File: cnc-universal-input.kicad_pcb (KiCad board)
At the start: 2 copper layers, 96.5 x 96.5 mm, 123 parts, among them J1 3PT, J10 2PT, J11 8PT, J12 USB_B_Mini, J13 2PT, J14 2PT, J2 3PT, J3 3PT, J4 3PT, J5 3PT, J6 3PT, J7 3PT, J8 3PT, J9 AVR-ISP-6, Q1 2N7002, Q11 2N7002, Q12 2N7002, Q13 2N7002, SW1 RESET, SW2 BTN, U1 ATmega328PB-AU, U10 SFH617A-4, U11 SFH617A-4, U12 SFH617A-4, U13 SFH617A-4, U14 SFH617A-4, U15 SFH617A-4, U16 SFH617A-4, U18 CH340G, U19 TS2596S, U2 74HC595, U3 74HC595, U4 74HC595, U5 4051, U6 TS2596S, U8 LM7321, U9 SFH617A-4, Y1 16MHz, Y2 12MHz

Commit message: Fixed missing and broken step files
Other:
- board text added: "IvyBit"
- board text added: "v1.5"
- board text removed: "IvyBit 2021"
- board text removed: "v1.4"
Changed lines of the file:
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@@
-(kicad_pcb (version 20171130) (host pcbnew "(5.1.8)-1")
+(kicad_pcb (version 20171130) (host pcbnew "(5.1.5)-3")
   (general
     (thickness 1.6)
@@
     (solder_mask_min_width 0.25)
     (aux_axis_origin 0 0)
-    (visible_elements 7FFFFFFF)
+    (visible_elements 7FFDFFFF)
     (pcbplotparams
       (layerselection 0x010fc_ffffffff)
@@
     (pad 1 smd rect (at -1.85 1.15 270) (size 1.9 1.1) (layers F.Cu F.Paste F.Mask)
       (net 2 "Net-(C2-Pad2)"))
-    (model ${KISYS3DMOD}/Crystal.3dshapes/Crystal_SMD_EuroQuartz_MJ-4Pin_5.0x3.2mm.wrl
+    (model ${KISYS3DMOD}/Crystal.3dshapes/Crystal_SMD_3225-4Pin_3.2x2.5mm.step
       (at (xyz 0 0 0))
-      (scale (xyz 1 1 1))
+      (scale (xyz 1.7 1.3 1))
       (rotate (xyz 0 0 0))
     )
@@
     (pad 1 smd rect (at -2.75 0 270) (size 1.5 2.4) (layers F.Cu F.Paste F.Mask)
       (net 78 "Net-(D21-Pad1)"))
-    (model ${KISYS3DMOD}/Inductor_SMD.3dshapes/L_6.3x6.3_H3.wrl
+    (model ${USERMOD}/Inductor_CD32.STEP
       (at (xyz 0 0 0))
-      (scale (xyz 1 1 1))
-      (rotate (xyz 0 0 0))
+      (scale (xyz 1.9 1.9 1.9))
+      (rotate (xyz 0 0 -90))
     )
   )
@@
     (pad 1 smd rect (at -2.75 0 90) (size 1.5 2.4) (layers F.Cu F.Paste F.Mask)
       (net 77 "Net-(D20-Pad1)"))
-    (model ${KISYS3DMOD}/Inductor_SMD.3dshapes/L_6.3x6.3_H3.wrl
+    (model ${USERMOD}/Inductor_CD32.STEP
       (at (xyz 0 0 0))
-      (scale (xyz 1 1 1))
-      (rotate (xyz 0 0 0))
+      (scale (xyz 1.8 1.8 1.8))
+      (rotate (xyz 0 0 -90))
     )
   )
@@
     (pad 1 thru_hole rect (at 0 0) (size 2.5 2.5) (drill 1.3) (layers *.Cu *.Mask)
       (net 4 +12V))
-    (model ${KISYS3DMOD}/TerminalBlock_RND.3dshapes/TerminalBlock_RND_205-00001_1x02_P5.00mm_Horizontal.wrl
-      (at (xyz 0 0 0))
+    (model "${USERMOD}/2er Terminal Block.step"
+      (offset (xyz 5 0 0))
       (scale (xyz 1 1 1))
-      (rotate (xyz 0 0 0))
+      (rotate (xyz 0 0 -180))
     )
   )
@@
     (pad 1 smd roundrect (at -2.625 -1.905 270) (size 1.65 0.6) (layers F.Cu F.Paste F.Mask) (roundrect_rratio 0.25)
       (net 3 +24V))
-    (model ${KISYS3DMOD}/Package_SO.3dshapes/SOP-8_3.9x4.9mm_P1.27mm.wrl
+    (model ${KISYS3DMOD}/Package_SO.3dshapes/SO-8_5.3x6.2mm_P1.27mm.wrl
       (at (xyz 0 0 0))
-      (scale (xyz 1 1 1))
+      (scale (xyz 0.8 1 0.5))
       (rotate (xyz 0 0 0))
     )
@@
     (pad 1 smd roundrect (at -2.625 -1.905 270) (size 1.65 0.6) (layers F.Cu F.Paste F.Mask) (roundrect_rratio 0.25)
       (net 3 +24V))
-    (model ${KISYS3DMOD}/Package_SO.3dshapes/SOP-8_3.9x4.9mm_P1.27mm.wrl
+    (model ${KISYS3DMOD}/Package_SO.3dshapes/SO-8_5.3x6.2mm_P1.27mm.wrl
       (at (xyz 0 0 0))
-      (scale (xyz 1 1 1))
+      (scale (xyz 0.8 1 0.5))
       (rotate (xyz 0 0 0))
     )
@@
     (pad 1 thru_hole rect (at 0 0) (size 2.5 2.5) (drill 1.3) (layers *.Cu *.Mask)
       (net 52 +5VD))
-    (model ${KISYS3DMOD}/TerminalBlock_RND.3dshapes/TerminalBlock_RND_205-00001_1x02_P5.00mm_Horizontal.wrl
-      (at (xyz 0 0 0))
+    (model "${USERMOD}/2er Terminal Block.step"
+      (offset (xyz 5 0 0))
       (scale (xyz 1 1 1))
-      (rotate (xyz 0 0 0))
+      (rotate (xyz 0 0 -180))
     )
   )
@@
     (pad 1 smd rect (at -3.975 -2.25 90) (size 1.55 1.3) (layers F.Cu F.Paste F.Mask)
       (net 1 GND))
-    (model ${KISYS3DMOD}/Button_Switch_SMD.3dshapes/SW_SPST_B3S-1000.wrl
+    (model ${USERMOD}/button_smd_6x6x4.3.stp
       (at (xyz 0 0 0))
       (scale (xyz 1 1 1))
-      (rotate (xyz 0 0 0))
+      (rotate (xyz 0 0 -90))
     )
   )
@@
     (pad 1 smd rect (at -3.975 -2.25 90) (size 1.55 1.3) (layers F.Cu F.Paste F.Mask)
       (net 1 GND))
-    (model ${KISYS3DMOD}/Button_Switch_SMD.3dshapes/SW_SPST_B3S-1000.wrl
+    (model ${USERMOD}/button_smd_6x6x4.3.stp
       (at (xyz 0 0 0))
       (scale (xyz 1 1 1))
-      (rotate (xyz 0 0 0))
+      (rotate (xyz 0 0 -90))
     )
   )
@@
     (pad 1 thru_hole rect (at 0 0) (size 2.5 2.5) (drill 1.3) (layers *.Cu *.Mask)
       (net 93 /BA))
-    (model ${KISYS3DMOD}/TerminalBlock_RND.3dshapes/TerminalBlock_RND_205-00007_1x08_P5.00mm_Horizontal.wrl
-      (at (xyz 0 0 0))
+    (model "${USERMOD}/8er Terminal Block.step"
+      (offset (xyz 35.2 0 0))
       (scale (xyz 1 1 1))
-      (rotate (xyz 0 0 0))
+      (rotate (xyz 0 0 -180))
     )
   )
@@
     (pad 1 thru_hole rect (at 0 0) (size 2.5 2.5) (drill 1.3) (layers *.Cu *.Mask)
       (net 3 +24V))
-    (model ${KISYS3DMOD}/TerminalBlock_RND.3dshapes/TerminalBlock_RND_205-00001_1x02_P5.00mm_Horizontal.wrl
-      (at (xyz 0 0 0))
+    (model "${USERMOD}/2er Terminal Block.step"
+      (offset (xyz 5 0 0))
       (scale (xyz 1 1 1))
-      (rotate (xyz 0 0 0))
+      (rotate (xyz 0 0 -180))
     )
   )
@@
     (pad 1 thru_hole rect (at 0 0 90) (size 2.5 2.5) (drill 1.3) (layers *.Cu *.Mask)
       (net 1 GND))
-    (model ${KISYS3DMOD}/TerminalBlock_RND.3dshapes/TerminalBlock_RND_205-00013_1x03_P5.00mm_Horizontal.wrl
-      (at (xyz 0 0 0))
+    (model "${USERMOD}/3er Terminal Block.step"
+      (offset (xyz 10 0 0))
       (scale (xyz 1 1 1))
-      (rotate (xyz 0 0 0))
+      (rotate (xyz 0 0 -180))
     )
   )
@@
     (pad 1 thru_hole rect (at 0 0 90) (size 2.5 2.5) (drill 1.3) (layers *.Cu *.Mask)
       (net 1 GND))
-    (model ${KISYS3DMOD}/TerminalBlock_RND.3dshapes/TerminalBlock_RND_205-00013_1x03_P5.00mm_Horizontal.wrl
-      (at (xyz 0 0 0))
+    (model "${USERMOD}/3er Terminal Block.step"
+      (offset (xyz 10 0 0))
       (scale (xyz 1 1 1))
-      (rotate (xyz 0 0 0))
+      (rotate (xyz 0 0 -180))
     )
   )
@@
     (pad 1 thru_hole rect (at 0 0 180) (size 2.5 2.5) (drill 1.3) (layers *.Cu *.Mask)
       (net 1 GND))
-    (model ${KISYS3DMOD}/TerminalBlock_RND.3dshapes/TerminalBlock_RND_205-00013_1x03_P5.00mm_Horizontal.wrl
-      (at (xyz 0 0 0))
+    (model "${USERMOD}/3er Terminal Block.step"
+      (offset (xyz 10 0 0))
       (scale (xyz 1 1 1))
-      (rotate (xyz 0 0 0))
+      (rotate (xyz 0 0 180))
     )
   )
@@
     (pad 1 thru_hole rect (at 0 0 180) (size 2.5 2.5) (drill 1.3) (layers *.Cu *.Mask)
       (net 1 GND))
-    (model ${KISYS3DMOD}/TerminalBlock_RND.3dshapes/TerminalBlock_RND_205-00013_1x03_P5.00mm_Horizontal.wrl
-      (at (xyz 0 0 0))
+    (model "${USERMOD}/3er Terminal Block.step"
+      (offset (xyz 10 0 0))
       (scale (xyz 1 1 1))
-      (rotate (xyz 0 0 0))
+      (rotate (xyz 0 0 -180))
     )
   )
@@
     (pad 1 thru_hole rect (at 0 0 180) (size 2.5 2.5) (drill 1.3) (layers *.Cu *.Mask)
       (net 1 GND))
-    (model ${KISYS3DMOD}/TerminalBlock_RND.3dshapes/TerminalBlock_RND_205-00013_1x03_P5.00mm_Horizontal.wrl
-      (at (xyz 0 0 0))
+    (model "${USERMOD}/3er Terminal Block.step"
+      (offset (xyz 10 0 0))
       (scale (xyz 1 1 1))
-      (rotate (xyz 0 0 0))
+      (rotate (xyz 0 0 -180))
     )
   )
@@
     (pad 1 thru_hole rect (at 0 0 180) (size 2.5 2.5) (drill 1.3) (layers *.Cu *.Mask)
       (net 1 GND))
-    (model ${KISYS3DMOD}/TerminalBlock_RND.3dshapes/TerminalBlock_RND_205-00013_1x03_P5.00mm_Horizontal.wrl
-      (at (xyz 0 0 0))
+    (model "${USERMOD}/3er Terminal Block.step"
+      (offset (xyz 10 0 0))
       (scale (xyz 1 1 1))
-      (rotate (xyz 0 0 0))
+      (rotate (xyz 0 0 -180))
     )
   )
@@
     (pad 1 thru_hole rect (at 0 0 270) (size 2.5 2.5) (drill 1.3) (layers *.Cu *.Mask)
       (net 1 GND))
-    (model ${KISYS3DMOD}/TerminalBlock_RND.3dshapes/TerminalBlock_RND_205-00013_1x03_P5.00mm_Horizontal.wrl
-      (at (xyz 0 0 0))
+    (model "${USERMOD}/3er Terminal Block.step"
+      (offset (xyz 10 0 0))
       (scale (xyz 1 1 1))
-      (rotate (xyz 0 0 0))
+      (rotate (xyz 0 0 -180))
     )
   )
@@
     (pad 1 thru_hole rect (at 0 0 270) (size 2.5 2.5) (drill 1.3) (layers *.Cu *.Mask)
       (net 1 GND))
-    (model ${KISYS3DMOD}/TerminalBlock_RND.3dshapes/TerminalBlock_RND_205-00013_1x03_P5.00mm_Horizontal.wrl
-      (at (xyz 0 0 0))
+    (model "${USERMOD}/3er Terminal Block.step"
+      (offset (xyz 10 0 0))
       (scale (xyz 1 1 1))
-      (rotate (xyz 0 0 0))
+      (rotate (xyz 0 0 -180))
     )
   )
@@
   (gr_circle (center 229.108 -77.216) (end 229.362 -77.216) (layer F.SilkS) (width 0.5))
   (gr_circle (center 250.19 -54.61) (end 250.444 -54.61) (layer F.SilkS) (width 0.5))
-  (gr_text "IvyBit 2021" (at 249.174 -59.944) (layer F.Mask)
+  (gr_text IvyBit (at 249.174 -59.944) (layer F.Mask)
     (effects (font (size 1 1) (thickness 0.127)))
   )
@@
     (effects (font (size 1.5 1.5) (thickness 0.3)))
   )
-  (gr_text v1.4 (at 243.078 -59.944) (layer F.Mask)
+  (gr_text v1.5 (at 245.11 -59.944) (layer F.Mask)
     (effects (font (size 1 1) (thickness 0.127)))
   )

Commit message: Cap be gone
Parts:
- removed C25: 10uF, Capacitor_SMD:CP_Elec_4x5.4
- removed C26: 100nF, Capacitor_SMD:C_0805_2012Metric
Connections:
- J12 pad 1: Net-(J12-Pad1) -> (no net)
- J12 pad 4: Net-(J12-Pad4) -> (no net)
- U1 pad 3: Net-(U1-Pad3) -> (no net)
- U1 pad 6: Net-(U1-Pad6) -> (no net)
- U18 pad 10: Net-(U18-Pad10) -> (no net)
- U18 pad 11: Net-(U18-Pad11) -> (no net)
- U18 pad 12: Net-(U18-Pad12) -> (no net)
- U18 pad 13: Net-(U18-Pad13) -> (no net)
- U18 pad 14: Net-(U18-Pad14) -> (no net)
- U18 pad 15: Net-(U18-Pad15) -> (no net)
- U18 pad 9: Net-(U18-Pad9) -> (no net)
- U2 pad 9: Net-(U2-Pad9) -> (no net)
- U3 pad 9: Net-(U3-Pad9) -> (no net)
- U8 pad 1: Net-(U8-Pad1) -> (no net)
- U8 pad 5: Net-(U8-Pad5) -> (no net)
- U8 pad 8: Net-(U8-Pad8) -> (no net)
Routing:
- net +5VD: track 38.1 -> 29.4 mm
- net /BE: track 45.9 -> 45.4 mm

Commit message: vias
removed most vias under pads
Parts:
- moved C6 168.7 mm to (104.3, 122.0)
- moved C1 168.7 mm to (112.6, 87.8)
- moved C10 168.7 mm to (185.0, 94.0)
- moved C11 168.7 mm to (170.3, 94.0)
- moved C12 168.7 mm to (170.3, 109.3)
- moved C13 168.7 mm to (176.0, 94.0)
- moved C14 168.7 mm to (117.0, 113.3)
- moved C19 168.7 mm to (116.9, 83.6)
- moved C22 168.7 mm to (123.4, 57.5)
- moved C23 168.7 mm to (136.0, 69.8)
- moved C3 168.7 mm to (104.3, 114.4)
- moved C5 168.7 mm to (159.8, 56.2)
- moved C7 168.7 mm to (104.3, 106.7)
- moved C8 168.7 mm to (117.0, 115.4)
- moved D10 168.7 mm to (165.9, 68.0)
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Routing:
- net +12V: track 347.4 -> 351.0 mm, vias 11 -> 13
- net /TO: track 22.0 -> 23.6 mm
- net /OUT-E: track 29.3 -> 30.7 mm
- net /OUT-G: track 28.3 -> 29.7 mm
- net /OUT-F: track 28.8 -> 30.1 mm
- net /OUT-H: track 28.4 -> 29.8 mm
- net /OUT-A: track 24.5 -> 25.4 mm
- net /OUT-D: track 26.2 -> 27.1 mm
- net /OUT-C: track 27.4 -> 28.2 mm
- net /OUT-B: track 27.4 -> 28.1 mm

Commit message: assemble all the things!
JLCPCB please make my life easier!!
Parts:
- removed J11: 8PT, TerminalBlock_RND:TerminalBlock_RND_205-00007_1x08_P5.00mm_Horizontal
- removed R72: 4.7K, Resistor_SMD:R_0805_2012Metric
- removed R73: 1.5K, Resistor_SMD:R_0805_2012Metric
- removed R74: 9.1K, Resistor_SMD:R_0805_2012Metric
- removed R75: 1K, Resistor_SMD:R_0805_2012Metric
- removed RN11, RN12: 470P4, Resistor_SMD:R_Array_Convex_4x0603
- added C25: 10uF, Capacitor_SMD:C_1206_3216Metric, F.Cu at (170.2, 96.0)
- added C26: 10uF, Capacitor_SMD:C_1206_3216Metric, F.Cu at (126.0, 45.0)
- added D27: LEDO, Diode_SMD:D_0805_2012Metric, F.Cu at (170.2, 100.6)
- added J15: 2PT, TerminalBlock_RND:TerminalBlock_RND_205-00001_1x02_P5.00mm_Horizontal, F.Cu at (135.3, 132.1)
- added J16: 2PT, TerminalBlock_RND:TerminalBlock_RND_205-00001_1x02_P5.00mm_Horizontal, F.Cu at (145.3, 132.1)
- added J17: 2PT, TerminalBlock_RND:TerminalBlock_RND_205-00001_1x02_P5.00mm_Horizontal, F.Cu at (155.3, 132.1)
- added J18: 2PT, TerminalBlock_RND:TerminalBlock_RND_205-00001_1x02_P5.00mm_Horizontal, F.Cu at (165.3, 132.1)
- added Q2: 2N7002, Package_TO_SOT_SMD:SOT-23, F.Cu at (141.6, 97.5)
- added Q3: 2N7002, Package_TO_SOT_SMD:SOT-23, F.Cu at (141.6, 101.1)
- added Q4: 2N7002, Package_TO_SOT_SMD:SOT-23, F.Cu at (141.6, 104.6)
- added Q5: 2N7002, Package_TO_SOT_SMD:SOT-23, F.Cu at (141.6, 108.2)
- added Q6: 2N7002, Package_TO_SOT_SMD:SOT-23, F.Cu at (141.6, 115.3)
- added Q7: 2N7002, Package_TO_SOT_SMD:SOT-23, F.Cu at (141.6, 111.8)
- added Q8: 2N7002, Package_TO_SOT_SMD:SOT-23, F.Cu at (141.6, 118.9)
- added Q9: 2N7002, Package_TO_SOT_SMD:SOT-23, F.Cu at (141.6, 122.4)
- added R1: 220, Resistor_SMD:R_0805_2012Metric, F.Cu at (162.6, 102.2)
- added R2: 220, Resistor_SMD:R_0805_2012Metric, F.Cu at (157.5, 102.2)
- added R3: 220, Resistor_SMD:R_0805_2012Metric, F.Cu at (152.4, 102.2)
- added R4: 220, Resistor_SMD:R_0805_2012Metric, F.Cu at (147.3, 102.2)
- added R5: 220, Resistor_SMD:R_0805_2012Metric, F.Cu at (157.5, 113.7)
- added R6: 220, Resistor_SMD:R_0805_2012Metric, F.Cu at (162.6, 113.7)
- added R7: 220, Resistor_SMD:R_0805_2012Metric, F.Cu at (152.4, 113.7)
- added R8: 220, Resistor_SMD:R_0805_2012Metric, F.Cu at (147.3, 113.7)
- added R9: 1K, Resistor_SMD:R_0805_2012Metric, F.Cu at (170.2, 98.3)
- added TP1: GND, TestPoint:TestPoint_Pad_D1.5mm, F.Cu at (113.0, 57.1)
- added TP2: +24V, TestPoint:TestPoint_Pad_D1.5mm, F.Cu at (126.4, 57.1)
- added TP3: +5V, TestPoint:TestPoint_Pad_D1.5mm, F.Cu at (117.5, 57.1)
- added TP4: +12V, TestPoint:TestPoint_Pad_D1.5mm, F.Cu at (121.9, 57.1)
- added U7: ADuM1201AR, Package_SO:SOIC-8_3.9x4.9mm_P1.27mm, F.Cu at (177.0, 93.0)
- BZ1: footprint Buzzer_Beeper:MagneticBuzzer_ProSignal_ABT-410-RC -> Buzzer_Beeper:Buzzer_15x7.5RM7.6
- C10, C5: value 10uF -> 100nF; footprint Capacitor_SMD:CP_Elec_4x5.4 -> Capacitor_SMD:C_0805_2012Metric
- C11, C12: value 30pF -> 22pF
- C14, C8: value 100nF -> 10uF; footprint Capacitor_SMD:C_0805_2012Metric -> Capacitor_SMD:C_1206_3216Metric
- C15, C24: value 10nF -> 10uF; footprint Capacitor_SMD:C_0805_2012Metric -> Capacitor_SMD:C_1206_3216Metric
- C22, C27, C28: footprint Capacitor_SMD:CP_Elec_4x5.4 -> Capacitor_SMD:C_1206_3216Metric
- C3: value 150uF -> 470uF; footprint Capacitor_SMD:CP_Elec_6.3x7.7 -> Capacitor_SMD:CP_Elec_10x10
- D20, D21: value B240F -> SS36-E3/57T
- L1, L2: footprint Inductor_SMD:L_6.3x6.3_H3 -> Inductor_SMD:L_12x12mm_H8mm
- RN1, RN2: value 10KP4 -> 4.7KP4
- RN3, RN4: value 470P4 -> 330P4
- RN5, RN6: value 470P4 -> 620P4
- SW1, SW2: footprint Button_Switch_SMD:SW_SPST_B3S-1000 -> Button_Switch_SMD:SW_SPST_TL3342
- U10, U11, U12, U13, U14, U15, U16, U9: value SFH617A-4 -> EL357NC; footprint Package_DIP:DIP-4_W7.62mm -> IvyBit-footprints:SOP-4_4.1x4.4x2.54P
- U19: value TS2596S -> XL1509-5E1; footprint Package_SO:SOP-8_3.9x4.9mm_P1.27mm -> Package_SO:SOIC-8_3.9x4.9mm_P1.27mm
- U6: value TS2596S -> XL1509-12E1; footprint Package_SO:SOP-8_3.9x4.9mm_P1.27mm -> Package_SO:SOIC-8_3.9x4.9mm_P1.27mm
- U8: value LM7321 -> SGMOP07CXS8G/TR
- Y1: footprint Crystal:Crystal_SMD_EuroQuartz_MJ-4Pin_5.0x3.2mm -> Crystal:Crystal_SMD_3225-4Pin_3.2x2.5mm
- Y2: footprint Crystal:Crystal_HC49-4H_Vertical -> Crystal:Crystal_SMD_3225-4Pin_3.2x2.5mm
- moved C14 74.6 mm to (146.3, 44.7), turned to 270 degrees
- moved C24 72.6 mm to (166.6, 45.0), turned to 270 degrees
- moved C5 45.7 mm to (177.0, 98.6), turned to 180 degrees
- moved C8 34.6 mm to (146.8, 97.8)
- moved R17 24.8 mm to (112.6, 78.1)
- moved U9 21.0 mm to (162.6, 108.0)
- moved L1 20.8 mm to (129.5, 104.1), turned to 0 degrees
- moved C15 19.4 mm to (122.2, 96.8), turned to 270 degrees
- moved D21 18.9 mm to (118.1, 122.6), turned to 180 degrees
- moved U10 17.8 mm to (157.5, 108.0)
- moved U19 17.3 mm to (118.1, 105.4), turned to 180 degrees
- moved C6 16.4 mm to (110.2, 106.7), turned to 270 degrees
- moved U15 16.2 mm to (152.4, 119.4)
- moved L2 16.1 mm to (129.5, 118.1), turned to 0 degrees
- moved U13 16.1 mm to (162.6, 119.4)
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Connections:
- C10 pad 1: +5V -> GND
- C10 pad 2: GND -> +5V
- C11 pad 1: GND -> GND_USB
- C12 pad 1: GND -> Net-(C12-Pad1)
- C12 pad 2: Net-(C12-Pad2) -> GND_USB
- C13 pad 2: GND -> GND_USB
- C15 pad 2: Net-(C15-Pad2) -> GND
- C21 pad 1: +5V -> VBUS
- C21 pad 2: GND -> GND_USB
- C24 pad 2: Net-(C24-Pad2) -> GND
- C5 pad 1: +5V -> GND_USB
- C5 pad 2: GND -> VBUS
- D18 pad 1: /RX -> /RX1
- D19 pad 1: /TX -> /TX1
- J12 pad 1: (no net) -> VBUS
- J12 pad 5: GND -> GND_USB
- R66 pad 1: +5V -> VBUS
- R67 pad 1: +5V -> VBUS
- U1 pad 30: /RX -> /RX2
- U1 pad 31: /TX -> /TX2
- U10 pad 1: /POB -> Net-(R2-Pad2)
- U10 pad 2: GND -> Net-(Q3-Pad3)
- U11 pad 1: /POC -> Net-(R3-Pad2)
- U11 pad 2: GND -> Net-(Q4-Pad3)
- U12 pad 1: /POD -> Net-(R4-Pad2)
- U12 pad 2: GND -> Net-(Q5-Pad3)
- U13 pad 1: /POE -> Net-(R6-Pad2)
- U13 pad 2: GND -> Net-(Q7-Pad3)
- U14 pad 1: /POF -> Net-(R5-Pad2)
- U14 pad 2: GND -> Net-(Q6-Pad3)
- U15 pad 1: /POG -> Net-(R7-Pad2)
- U15 pad 2: GND -> Net-(Q8-Pad3)
- U16 pad 1: /POH -> Net-(R8-Pad2)
- U16 pad 2: GND -> Net-(Q9-Pad3)
- U18 pad 1: GND -> GND_USB
- U18 pad 16: +5V -> VBUS
- U18 pad 2: /RX -> /RX1
- U18 pad 3: /TX -> /TX1
- U18 pad 7: Net-(C11-Pad2) -> Net-(C12-Pad1)
- U18 pad 8: Net-(C12-Pad2) -> Net-(C11-Pad2)
- U19 pad 3: Net-(C15-Pad2) -> +5V
- U6 pad 3: Net-(C24-Pad2) -> +12V
- U9 pad 1: /POA -> Net-(R1-Pad2)
- U9 pad 2: GND -> Net-(Q2-Pad3)
- Y2 pad 1: Net-(C12-Pad2) -> Net-(C11-Pad2)
- Y2 pad 2: Net-(C11-Pad2) -> GND_USB
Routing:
- net +5V: track 282.7 -> 377.0 mm
- net /TX: track 80.7 -> 0.00 mm, vias 2 -> 0
- net /RX: track 77.2 -> 0.00 mm, vias 2 -> 0
- net /RX2: track 0.00 -> 65.0 mm, vias 0 -> 2
- net /TX2: track 0.00 -> 64.1 mm, vias 0 -> 2
- net +12V: track 351.0 -> 397.9 mm, vias 13 -> 14
- net GND: track 2.33 -> 47.9 mm, vias 297 -> 252
- net VBUS: track 0.00 -> 40.5 mm, vias 0 -> 1
- net /TX1: track 0.00 -> 29.7 mm, vias 0 -> 2
- net /RX1: track 0.00 -> 29.5 mm, vias 0 -> 2
- net Net-(Q7-Pad3): track 0.00 -> 27.5 mm
- net /BD: track 34.1 -> 60.4 mm, vias 1 -> 2
- net Net-(Q2-Pad3): track 0.00 -> 25.2 mm
- net Net-(Q6-Pad3): track 0.00 -> 24.9 mm
- net Net-(C24-Pad2): track 22.6 -> 0.00 mm
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- added copper zone on B.Cu, net GND_USB
- added copper zone on F.Cu, net GND_USB
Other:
- outline, holes or cut-outs redrawn
- board text added: "15-36V"
- board text added: "3.5mm"
- board text added: "RESET"
- board text added: "v1.6"
- board text removed: "16-30V"
- board text removed: "3.4mm"
- board text removed: "UCNC"
- board text removed: "v1.5"

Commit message: Update cnc-universal-input.kicad_pcb
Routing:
- net /OUT-C: track 26.5 -> 25.9 mm

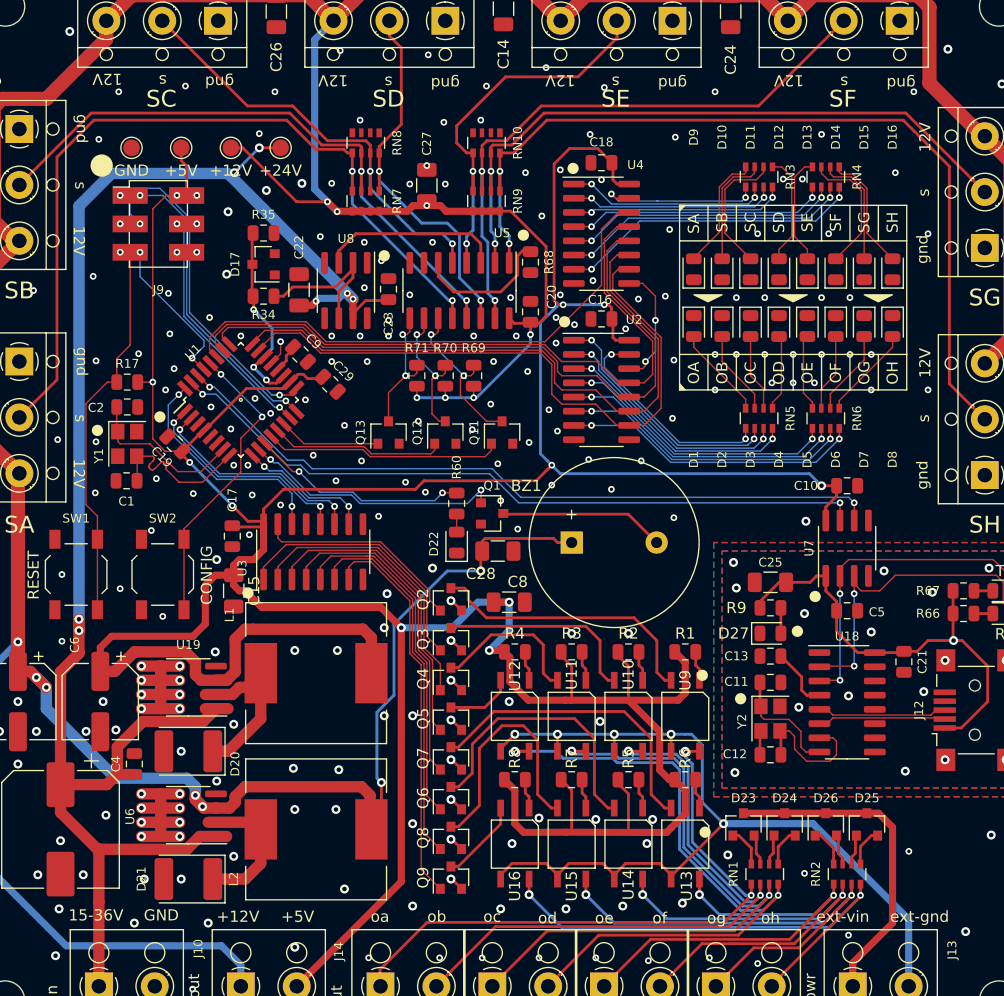
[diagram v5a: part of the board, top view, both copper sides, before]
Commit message: Keep something in stock ffs...
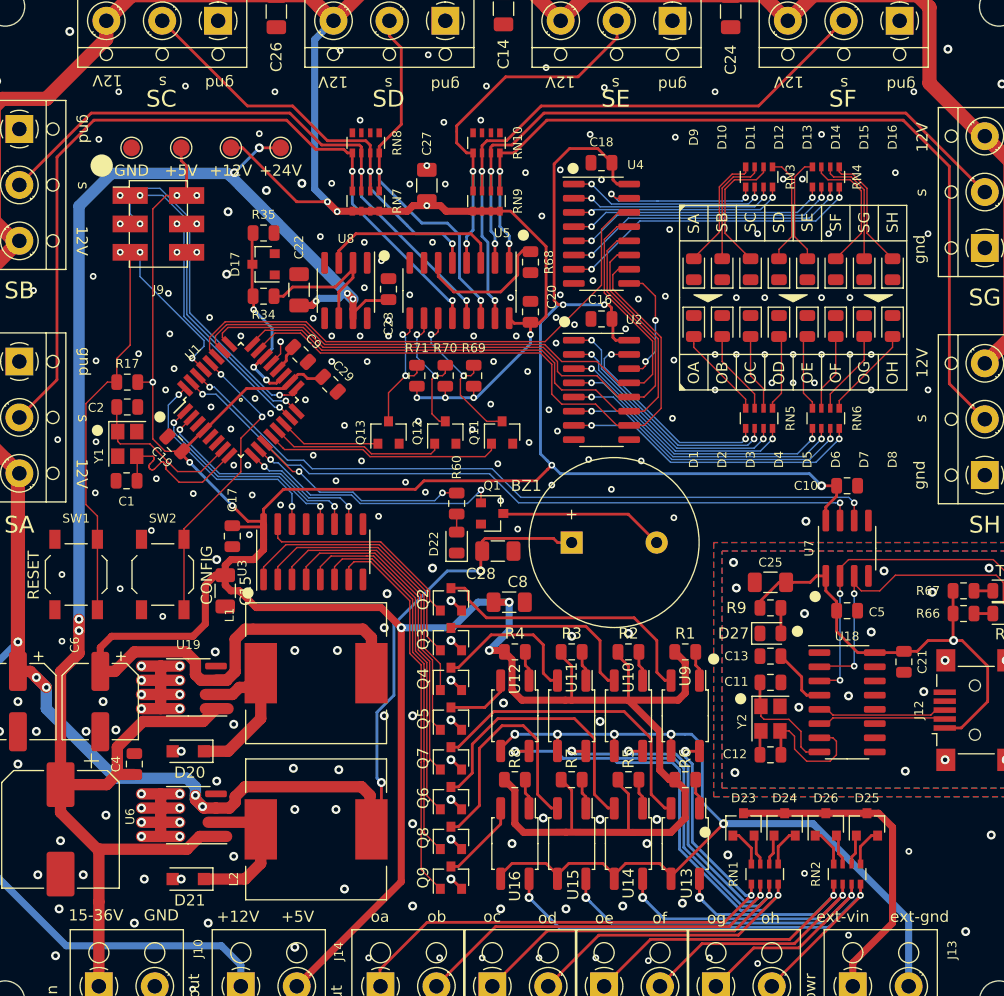
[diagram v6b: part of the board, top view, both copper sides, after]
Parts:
- D20, D21: value SS36-E3/57T -> DSK36; footprint Diode_SMD:D_2114_3652Metric -> Diode_SMD:D_SOD-123F
- U10, U11, U12, U13, U14, U15, U16, U9: footprint IvyBit-footprints:SOP-4_4.1x4.4x2.54P -> Package_SO:SO-4_4.4x3.9mm_P2.54mm
- U8: value SGMOP07CXS8G/TR -> TL071CDR
- moved C15 0.76 mm to (121.4, 96.8)
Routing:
- net +5V: track 377.0 -> 377.9 mm
- net Net-(D21-Pad1): track 13.1 -> 13.9 mm
- net Net-(D20-Pad1): track 16.3 -> 17.1 mm
- net GND: vias 252 -> 253
